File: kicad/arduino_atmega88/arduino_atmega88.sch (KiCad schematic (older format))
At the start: 22 parts, among them IC1 ATMEGA88A-A, P1 CONN_6, P2 CONN_1, P3 CONN_1, P4 CONN_7, SW1 SW_PUSH, U1 78L05, X1 16MHz

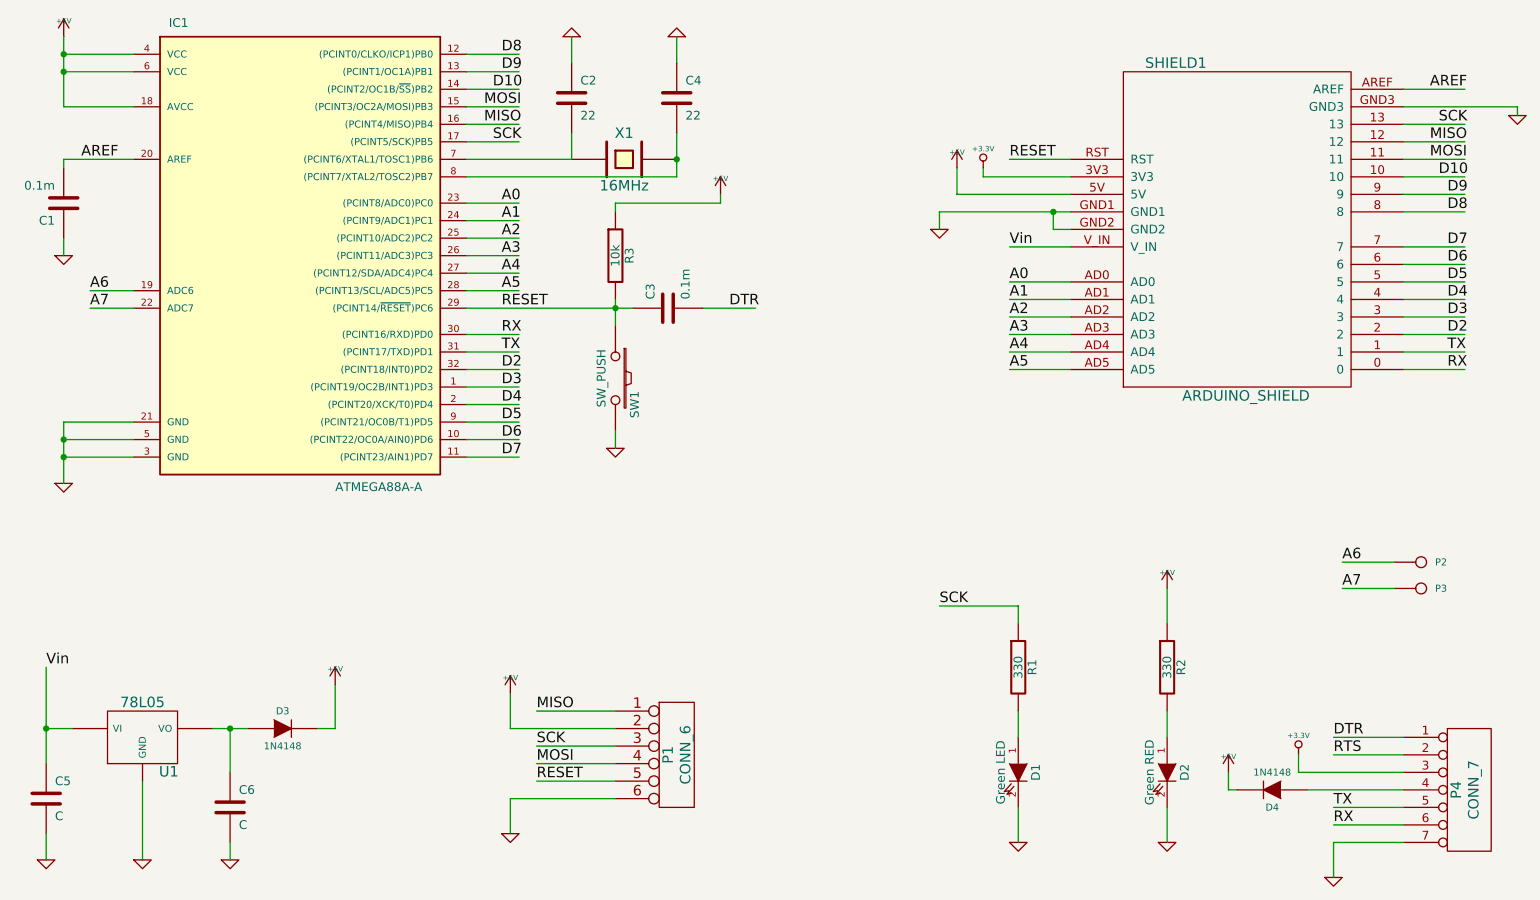
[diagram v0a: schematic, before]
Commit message: 1M resistor on Xtal
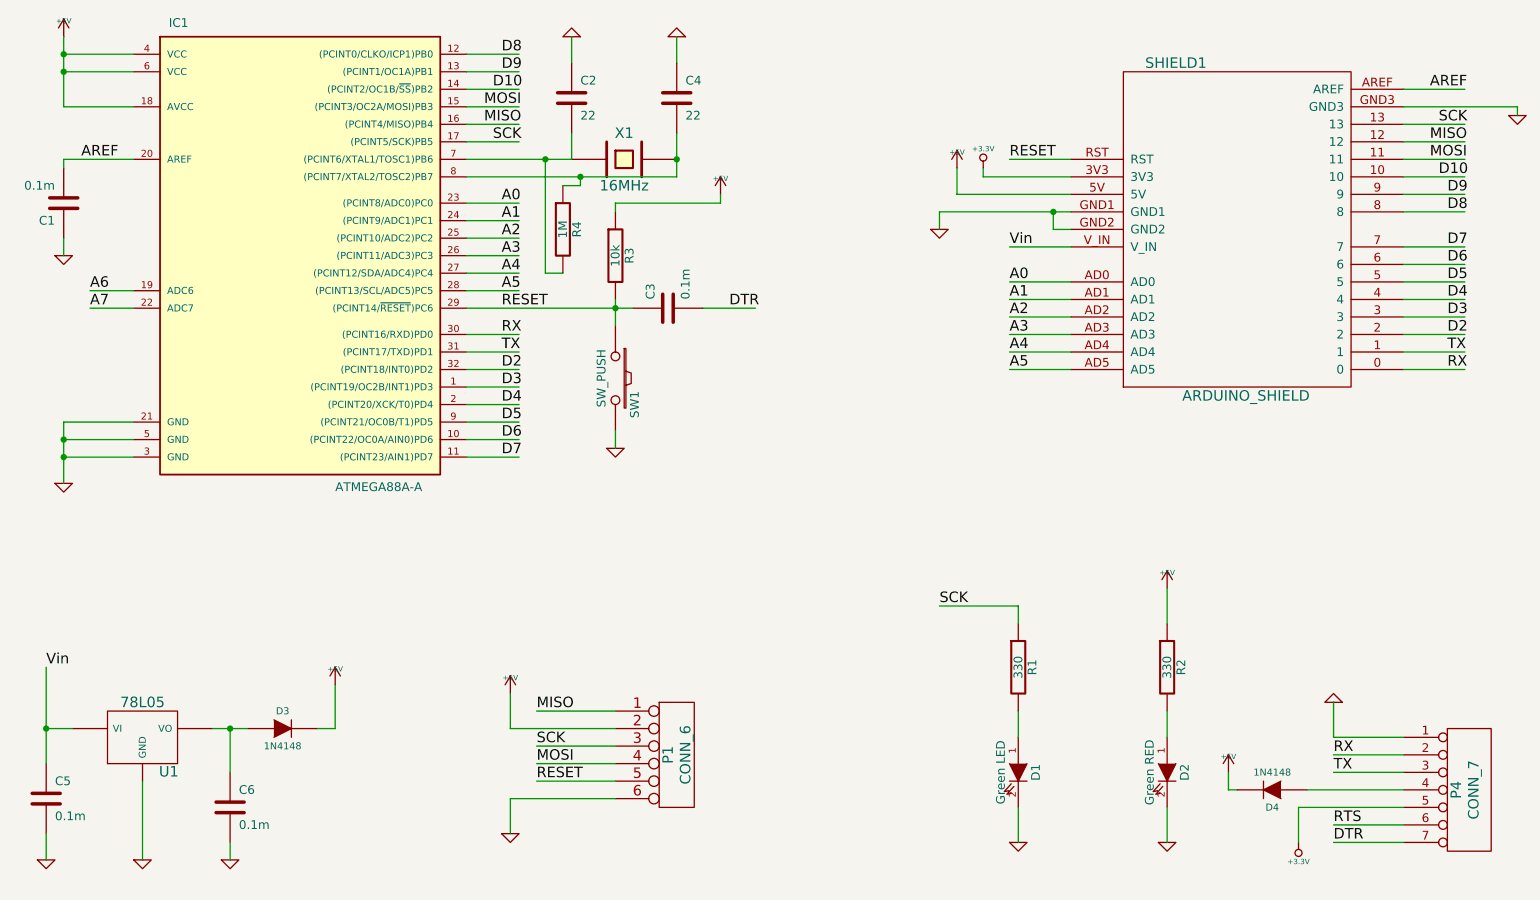
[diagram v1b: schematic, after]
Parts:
- removed P2, P3: CONN_1, symbol CONN_1
- added R4: 1M, symbol R
- C5, C6: value C -> 0.1m
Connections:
- wire segments 116 -> 118

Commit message: just update to rescue library, why kicad is doing this???
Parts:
- C1, C2, C3, C4, C5, C6: symbol C -> C-RESCUE-arduino_atmega88
- D1, D2: symbol LED -> LED-RESCUE-arduino_atmega88
- R1, R2, R3, R4: symbol R -> R-RESCUE-arduino_atmega88
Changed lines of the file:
@@
 EESchema Schematic File Version 2
+LIBS:arduino_atmega88-rescue
 LIBS:power
 LIBS:device
@@
 LIBS:memory
 LIBS:xilinx
-LIBS:special
 LIBS:microcontrollers
 LIBS:dsp
@@
 $EndComp
 $Comp
-L GND #PWR01
+L GND-RESCUE-arduino_atmega88 #PWR01
 U 1 1 5335A5BD
 P 2200 6100
@@
 $EndComp
 $Comp
-L GND #PWR02
+L GND-RESCUE-arduino_atmega88 #PWR02
 U 1 1 5335A5B8
 P 2700 6100
@@
 $EndComp
 $Comp
-L GND #PWR03
+L GND-RESCUE-arduino_atmega88 #PWR03
 U 1 1 5335A5B7
 P 1650 6100
@@
 $EndComp
 $Comp
-L C C6
+L C-RESCUE-arduino_atmega88 C6
 U 1 1 5335A584
 P 2700 5800
@@
 $EndComp
 $Comp
-L C C5
+L C-RESCUE-arduino_atmega88 C5
 U 1 1 5335A581
 P 1650 5750
@@
 $EndComp
 $Comp
-L LED D2
+L LED-RESCUE-arduino_atmega88 D2
 U 1 1 53318026
 P 8050 5600
@@
 $EndComp
 $Comp
-L R R2
+L R-RESCUE-arduino_atmega88 R2
 U 1 1 53318025
 P 8050 5000
@@
 $EndComp
 $Comp
-L GND #PWR06
+L GND-RESCUE-arduino_atmega88 #PWR06
 U 1 1 53318024
 P 8050 6000
@@
 SCK
 $Comp
-L GND #PWR07
+L GND-RESCUE-arduino_atmega88 #PWR07
 U 1 1 53317FD6
 P 7200 6000
@@
 $EndComp
 $Comp
-L R R1
+L R-RESCUE-arduino_atmega88 R1
 U 1 1 53317FCD
 P 7200 5000
@@
 $EndComp
 $Comp
-L LED D1
+L LED-RESCUE-arduino_atmega88 D1
 U 1 1 53317FC2
 P 7200 5600
@@
 DTR
 $Comp
-L +3.3V #PWR08
+L +3.3V-RESCUE-arduino_atmega88 #PWR08
 U 1 1 53317D04
 P 8800 6000
@@
 RX
 $Comp
-L GND #PWR010
+L GND-RESCUE-arduino_atmega88 #PWR010
 U 1 1 53317C3C
 P 9000 5200
@@
 MOSI
 $Comp
-L GND #PWR011
+L GND-RESCUE-arduino_atmega88 #PWR011
 U 1 1 53317586
 P 4300 5950
@@
 $EndComp
 $Comp
-L GND #PWR013
+L GND-RESCUE-arduino_atmega88 #PWR013
 U 1 1 53317494
 P 1750 3950
@@
 AREF
 $Comp
-L GND #PWR015
+L GND-RESCUE-arduino_atmega88 #PWR015
 U 1 1 53317195
 P 1750 2650
@@
 $EndComp
 $Comp
-L C C1
+L C-RESCUE-arduino_atmega88 C1
 U 1 1 5331718F
 P 1750 2350
@@
 AREF
 $Comp
-L GND #PWR016
+L GND-RESCUE-arduino_atmega88 #PWR016
 U 1 1 53317146
 P 10050 1850
@@
 Vin
 $Comp
-L GND #PWR017
+L GND-RESCUE-arduino_atmega88 #PWR017
 U 1 1 533170E1
 P 6750 2500
@@
 $EndComp
 $Comp
-L +3.3V #PWR019
+L +3.3V-RESCUE-arduino_atmega88 #PWR019
 U 1 1 533170BB
 P 7000 2150
@@
 RX
 $Comp
-L GND #PWR020
+L GND-RESCUE-arduino_atmega88 #PWR020
 U 1 1 53316F0E
 P 4900 3750
@@
 $EndComp
 $Comp
-L R R3
+L R-RESCUE-arduino_atmega88 R3
 U 1 1 53316DE9
 P 4900 2650
@@
 DTR
 $Comp
-L C C3
+L C-RESCUE-arduino_atmega88 C3
 U 1 1 53316DBF
 P 5200 2950
@@
 A0
 $Comp
-L GND #PWR022
+L GND-RESCUE-arduino_atmega88 #PWR022
 U 1 1 53316CEE
 P 5250 1400
@@
 $EndComp
 $Comp
-L GND #PWR023
+L GND-RESCUE-arduino_atmega88 #PWR023
 U 1 1 53316CAD
 P 4650 1400
@@
 $EndComp
 $Comp
-L C C4
+L C-RESCUE-arduino_atmega88 C4
 U 1 1 53316C9F
 P 5250 1750
@@
 $EndComp
 $Comp
-L C C2
+L C-RESCUE-arduino_atmega88 C2
 U 1 1 53316C9B
 P 4650 1750
@@
 $EndComp
 $Comp
-L R R4
+L R-RESCUE-arduino_atmega88 R4
 U 1 1 5452671C
 P 4600 2500
